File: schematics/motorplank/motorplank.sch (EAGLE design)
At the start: 17 parts, among them IC1 74AHC1G86DBV

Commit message: Tweaks to planks; change 0604 parts for 0805 where possible
Also added 4 pin plank; minor text changes.
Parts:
- C1, C2: device SparkFun-Passives:CAP0603-CAP -> SparkFun-Passives:CAP0805
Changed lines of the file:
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@@
 <part name="+3V4" library="supply1" deviceset="+3V3" device=""/>
 <part name="GND7" library="supply1" deviceset="GND" device=""/>
-<part name="C1" library="SparkFun-Passives" deviceset="CAP" device="0603-CAP" value="0.1u"/>
-<part name="C2" library="SparkFun-Passives" deviceset="CAP" device="0603-CAP" value="0.1u"/>
+<part name="C1" library="SparkFun-Passives" deviceset="CAP" device="0805" value="0.1u"/>
+<part name="C2" library="SparkFun-Passives" deviceset="CAP" device="0805" value="0.1u"/>
 <part name="C3" library="SparkFun-Passives" deviceset="CAP_POL" device="C" value="10u"/>
 <part name="GND8" library="supply1" deviceset="GND" device=""/>

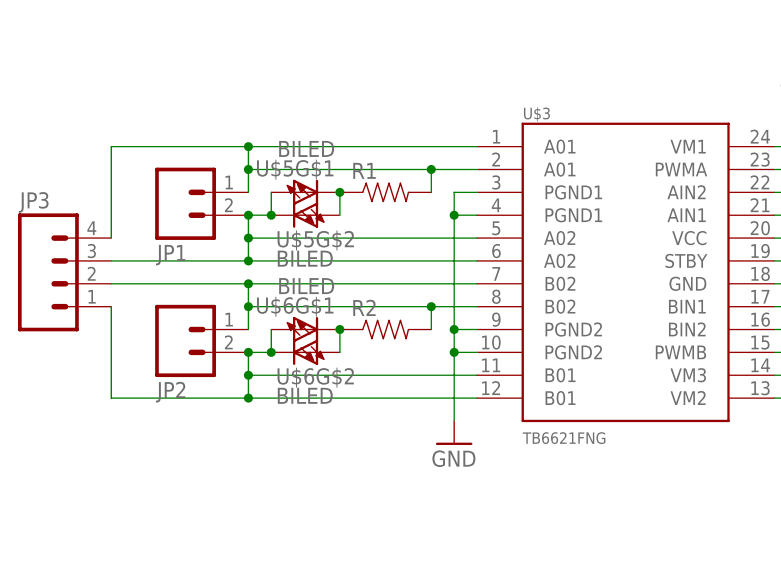
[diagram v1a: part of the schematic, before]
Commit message: Layout tweaks to motor plank.
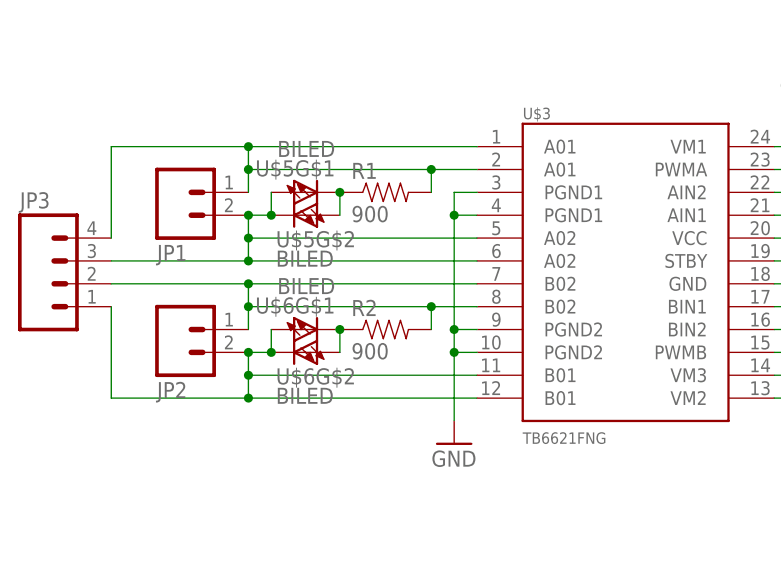
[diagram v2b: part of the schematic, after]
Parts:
- R1, R2: value (none) -> 900
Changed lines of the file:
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@@
 <part name="U$5" library="nickparts" deviceset="BILED" device=""/>
 <part name="U$6" library="nickparts" deviceset="BILED" device=""/>
-<part name="R1" library="SparkFun-Passives" deviceset="RESISTOR" device="0805-RES"/>
-<part name="R2" library="SparkFun-Passives" deviceset="RESISTOR" device="0805-RES"/>
+<part name="R1" library="SparkFun-Passives" deviceset="RESISTOR" device="0805-RES" value="900"/>
+<part name="R2" library="SparkFun-Passives" deviceset="RESISTOR" device="0805-RES" value="900"/>
 </parts>
 <sheets>
